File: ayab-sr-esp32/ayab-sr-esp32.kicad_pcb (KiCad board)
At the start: 2 copper layers, 64.5 x 83.1 mm, 65 parts, among them J1 USB_C_Receptacle_USB2.0_16P, J14 Conn_01x08, J2 USB_C_Receptacle_USB2.0_16P, J3 DIN-7, J4 Conn_01x02, Q1 BSS138, U1 CH224A, U10 AP2112K-3.3, U2 USBLC6-2SC6, U3 ESP32-S3-WROOM-1, U4 74AHCT1G125, U5 HS91L02W2C01, U6 TPS54202, U7 INA381A1, U8 74LVC125, U9 TPS54202

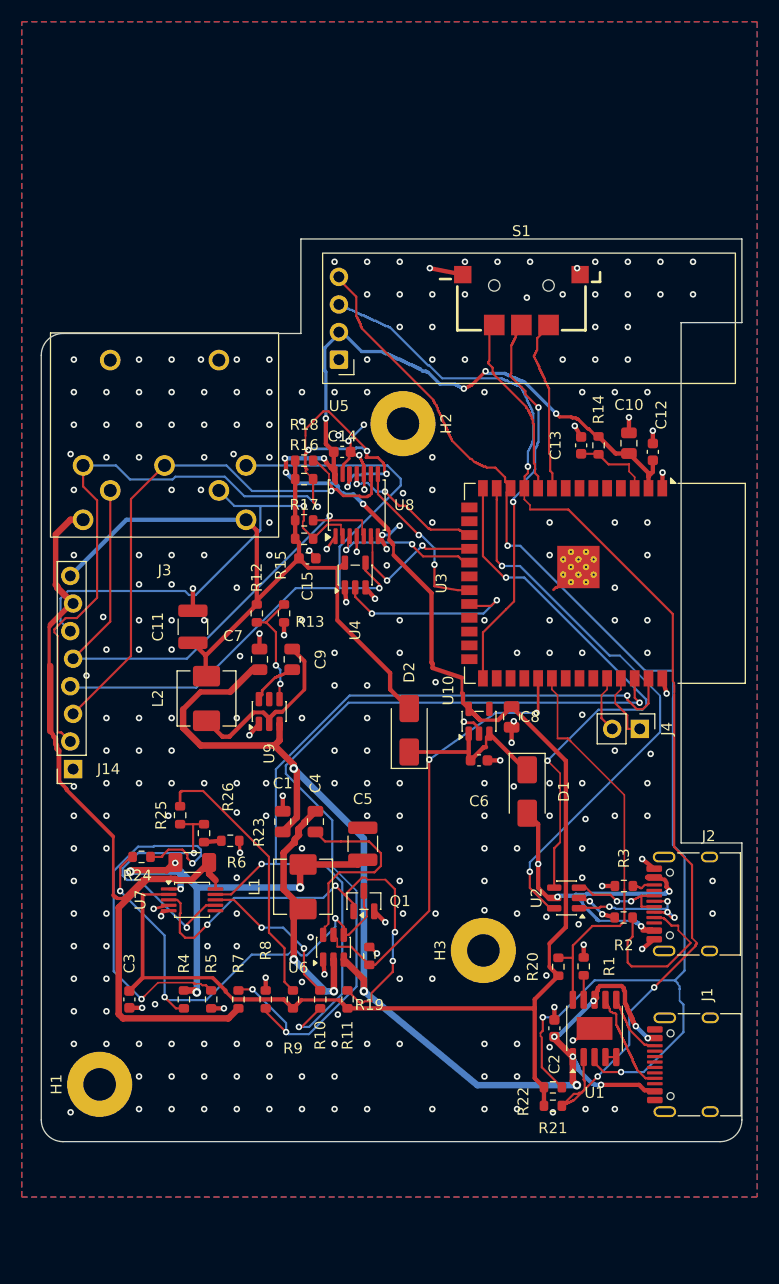
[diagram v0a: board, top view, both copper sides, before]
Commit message: ayab-sr-esp32: board 6 mm longer at the bottom, OLED clear of the antenna keep-out
J3, U5 and S1 and the top edge stay in place; everything else (ESP32 with
its antenna cut-out and keep-out, USB-C, mounting holes...) moves down 6 mm.
Tracks crossing the boundary get vertical extensions; the six DIN-side
tracks cut by it were rerouted. DRC now clean (the U5-in-keep-out item is
gone), connectivity identical. Production files, renders and viewer GLB
regenerated; the enclosure is not updated yet.

Co-Authored-By: Claude Opus 5.5 <noreply@anthropic.com>
Claude-Session: https://claude.ai/code/session_013hjzppJpAsDjhGU3Z3soKr
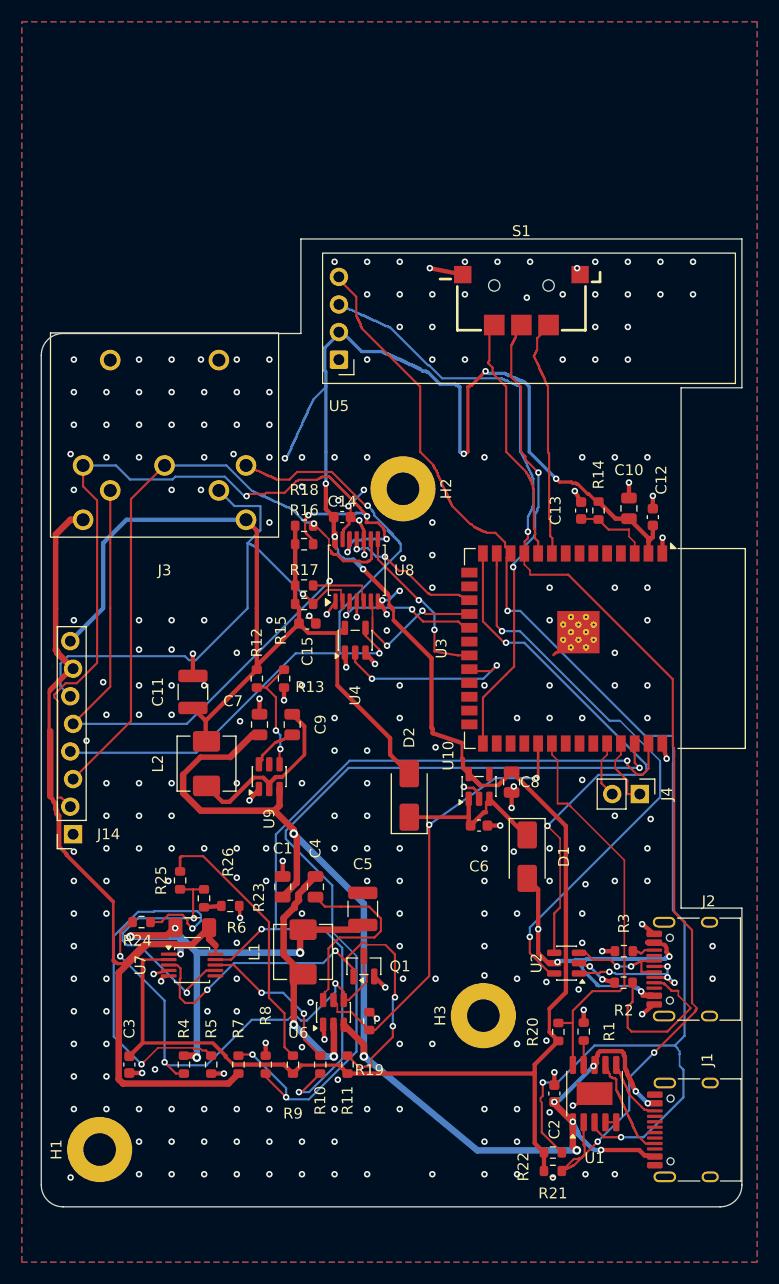
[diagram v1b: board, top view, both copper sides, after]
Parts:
- moved C11 6.00 mm to (114.0, 66.7)
- moved C7 6.00 mm to (120.1, 69.7)
- moved C9 6.00 mm to (123.1, 69.7)
- moved C1 6.00 mm to (122.2, 84.6)
- moved C10 6.00 mm to (154.1, 49.8)
- moved C12 6.00 mm to (156.3, 50.6)
- moved C13 6.00 mm to (149.7, 50.0)
- moved C14 6.00 mm to (127.7, 50.6)
- moved C15 6.00 mm to (124.5, 60.4)
- moved C2 6.00 mm to (147.2, 103.7)
- moved C3 6.00 mm to (108.1, 101.0)
- moved C4 6.00 mm to (125.2, 84.6)
- moved C5 6.00 mm to (129.6, 86.7)
- moved C6 6.00 mm to (140.3, 79.0)
- moved C8 6.00 mm to (143.3, 75.0)
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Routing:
- net +3.3V: track 191.4 -> 214.4 mm, vias 8 -> 7
- net +5V: track 71.9 -> 83.9 mm
- net /ND1: track 87.1 -> 96.4 mm
- net /HOK: track 43.0 -> 50.1 mm
- net /Vsol: track 78.6 -> 84.6 mm
- net /SDA: track 118.2 -> 124.2 mm
- net /CCP: track 52.4 -> 58.4 mm
- net /BTN_D: track 17.1 -> 23.1 mm
- net /BTN_C: track 36.2 -> 42.2 mm
- net /BTN_B: track 16.2 -> 22.2 mm
- net /SCL: track 106.8 -> 112.8 mm
- net /KSL: track 52.7 -> 58.2 mm
- net /DOB: track 62.3 -> 67.4 mm, vias 1 -> 2
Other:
- board size 64.5 x 83.1 mm -> 64.5 x 89.1 mm

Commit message: ayab-sr-esp32: OLED on a low-profile socket, enclosure post under its far end
- J15: 1x4 2.54 mm female socket, 5.0 mm high (HC-PM254-5.0H-1x4PZ-02A,
  LCSC C42163122), on U5's former pads. U5 keeps its symbol (BOM, LCSC
  C5248081) with a pad-less footprint (outline, courtyard, 3D model raised
  5 mm) and is left out of the placement file: it is plugged in by hand.
- New library footprints and a generated STEP model for the socket.
- 3.6 mm hole in the PCB under the OLED's far end (161.0, 32.3) for a
  post of the tray; one GND stitching via removed for edge clearance.
- Enclosure: updated for the 6 mm longer board (holes, USB-C), 3 mm post
  from the tray floor up to 0.1 mm under the module, lid ceiling raised
  by 5 mm (12.8 mm) to clear the OLED glass (11.74 mm). Fit check: no
  collision. Sections redone in the current board frame, plus one through
  the post.
- DRC 0, ERC 0, pad-net check OK; connectivity changes only by J15.
  Production files, renders and viewer regenerated.

Co-Authored-By: Claude Opus 5.5 <noreply@anthropic.com>
Claude-Session: https://claude.ai/code/session_013hjzppJpAsDjhGU3Z3soKr
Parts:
- added J15: HC-PM254-5.0H-1x4PZ-02A, Library:PinSocket_1x04_P2.54mm_Vertical_H5.0, F.Cu at (127.4, 36.1)
- U5: footprint Display:ER_OLEDM0.91_1x-I2C -> Library:OLED_0.91_128x32_I2C_Module_Socket_H5.0
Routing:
- net GND: vias 274 -> 273
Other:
- outline, holes or cut-outs redrawn

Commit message: ayab-sr-esp32: CH224A off the I2C bus, PCB cut under the OLED end, rectangular support block
- U1 CFG2/CFG3 no longer on SCL/SDA (no-connect flags): single-resistor
  mode, R1 alone requests 15 V. The bus serves the OLED only, so the display
  works with only J2 plugged in (an unpowered CH224A would hold the bus at
  ~2 V). Old U1 SDA/SCL tracks removed. Sheet notes and README updated
  (pin map, firmware notes, J2-only operation and PD-adapter-in-J2 detection).
- PCB cut along the antenna cut-out line (x = 158.9) up to the top edge;
  the round post hole is gone. One off-board stitching via removed.
- Enclosure: the OLED's overhanging far end rests on a rectangular block of
  the tray (x 159.3-165.0, y 27.0-37.6, joined to the side wall, 0.1 mm
  under the module). Fit check: no collision. Renders and sections redone.
- DRC 0, ERC 0. Connectivity change: SCL/SDA lose U1.2/U1.3 only.

Co-Authored-By: Claude Opus 5.5 <noreply@anthropic.com>
Claude-Session: https://claude.ai/code/session_013hjzppJpAsDjhGU3Z3soKr
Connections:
- U1 pad 2: /SCL -> unconnected-(U1-CFG2-Pad2)
- U1 pad 3: /SDA -> unconnected-(U1-CFG3-Pad3)
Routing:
- net /SDA: track 124.2 -> 108.5 mm, vias 3 -> 2
- net /SCL: track 112.8 -> 109.8 mm
- net GND: vias 273 -> 272
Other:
- outline, holes or cut-outs redrawn
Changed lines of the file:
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@@
 			(layers "F.Cu" "F.Mask" "F.Paste")
 			(roundrect_rratio 0.25)
-			(net "/SCL")
+			(net "unconnected-(U1-CFG2-Pad2)")
 			(pinfunction "CFG2_2")
-			(pintype "passive")
+			(pintype "passive+no_connect")
 		)
 		(pad "3" smd roundrect
@@
 			(layers "F.Cu" "F.Mask" "F.Paste")
 			(roundrect_rratio 0.25)
-			(net "/SDA")
+			(net "unconnected-(U1-CFG3-Pad3)")
 			(pinfunction "CFG3_3")
-			(pintype "passive")
+			(pintype "passive+no_connect")
 		)
 		(pad "4" smd roundrect
@@
 	(gr_line
 		(start 123.900001 24.999999)
-		(end 164.500001 24.999999)
-		(stroke
-			(width 0.05)
-			(type default)
-		)
-		(layer "Edge.Cuts")
-	)
-	(gr_line
-		(start 158.900001 38.699999)
-		(end 164.500001 38.699999)
+		(end 158.900001 24.999999)
 		(stroke
 			(width 0.05)
@@
 	(gr_line
 		(start 158.900001 86.599999)
-		(end 158.900001 38.699999)
+		(end 158.900001 24.999999)
 		(stroke
 			(width 0.05)
@@
 		(layer "Edge.Cuts")
 	)
-	(gr_circle
-		(center 161 32.3)
-		(end 162.8 32.3)
-		(stroke
-			(width 0.05)
-			(type default)
-		)
-		(fill no)
-		(layer "Edge.Cuts")
-	)
 	(gr_line
 		(start 162.500001 114.099999)
@@
 	)
 	(gr_line
-		(start 164.500001 38.699999)
-		(end 164.500001 24.999999)
-		(stroke
-			(width 0.05)
-			(type default)
-		)
-		(layer "Edge.Cuts")
-	)
-	(gr_line
 		(start 164.500001 86.599999)
 		(end 158.900001 86.599999)
@@
 	)
 	(via
-		(at 160.000001 27.099999)
-		(size 0.6)
-		(drill 0.3)
-		(layers "F.Cu" "B.Cu")
-		(net "GND")
-	)
-	(via
 		(at 118.300001 87.499999)
 		(size 0.6)
@@
 	)
 	(segment
-		(start 149.925001 106.299999)
-		(end 149.925001 108.399999)
-		(width 0.2)
-		(layer "F.Cu")
-		(net "/SCL")
-	)
-	(segment
 		(start 148.825001 110.399999)
 		(end 148.725001 110.399999)
@@
 	)
 	(segment
-		(start 149.925001 108.399999)
-		(end 150.025001 108.499999)
-		(width 0.2)
-		(layer "F.Cu")
-		(net "/SCL")
-	)
-	(segment
 		(start 147.925001 110.799999)
 		(end 149.025001 109.699999)
@@
 	)
 	(segment
-		(start 150.025001 108.499999)
-		(end 150.025001 109.299999)
-		(width 0.2)
-		(layer "F.Cu")
-		(net "/SCL")
-	)
-	(segment
 		(start 158.265001 72.973299)
 		(end 158.276901 72.961399)
@@
 	)
 	(segment
-		(start 150.935001 106.314999)
-		(end 150.935001 106.853899)
-		(width 0.2)
-		(layer "F.Cu")
-		(net "/SDA")
-	)
-	(segment
 		(start 137.700001 49.249999)
 		(end 137.600001 49.149999)
@@
 	)
 	(segment
-		(start 151.775201 107.694099)
-		(end 153.377101 107.694099)
-		(width 0.2)
-		(layer "F.Cu")
-		(net "/SDA")
-	)
-	(segment
 		(start 136.800001 47.249999)
 		(end 136.700001 47.149999)
@@
 	)
 	(segment
-		(start 150.935001 106.853899)
-		(end 151.775201 107.694099)
-		(width 0.2)
-		(layer "F.Cu")
-		(net "/SDA")
-	)
-	(segment
 		(start 129.200001 32.518199)
 		(end 129.200001 32.418199)
@@
 		(net "/SDA")
 	)
-	(via
-		(at 153.377101 107.694099)
-		(size 0.6)
-		(drill 0.3)
-		(layers "F.Cu" "B.Cu")
-		(net "/SDA")
-	)
-	(segment
-		(start 158.848801 101.211099)
-		(end 158.758001 101.120299)
-		(width 0.15)
-		(layer "B.Cu")
-		(net "/SDA")
-	)
-	(segment
-		(start 159.116201 101.478499)
-		(end 158.848801 101.211099)
-		(width 0.2)
-		(layer "B.Cu")
-		(net "/SDA")
-	)
 	(segment
 		(start 147.528401 102.653199)
@@
 	)
 	(segment
-		(start 158.765901 100.051599)
-		(end 158.765901 99.784299)
-		(width 0.2)
-		(layer "B.Cu")
-		(net "/SDA")
-	)
-	(segment
 		(start 150.932901 99.248699)
 		(end 147.528401 102.653199)
@@
 	)
 	(segment
-		(start 158.758001 100.059499)
-		(end 158.765901 100.051599)
-		(width 0.2)
-		(layer "B.Cu")
-		(net "/SDA")
-	)
-	(segment
 		(start 155.593801 70.743599)
 		(end 158.147801 70.743599)
@@
 	)
 	(segment
-		(start 158.758001 101.120299)
-		(end 158.758001 100.059499)
-		(width 0.15)
-		(layer "B.Cu")
-		(net "/SDA")
-	)
-	(segment
 		(start 158.147801 70.743599)
 		(end 158.147801 73.243999)
@@
 	)
 	(segment
-		(start 159.116201 104.020799)
-		(end 159.116201 101.478499)
-		(width 0.2)
-		(layer "B.Cu")
-		(net "/SDA")
-	)
-	(segment
 		(start 158.147801 86.793499)
 		(end 158.147801 73.243999)
@@
 	)
 	(segment
-		(start 153.377101 107.694099)
-		(end 155.442901 107.694099)
-		(width 0.2)
-		(layer "B.Cu")
-		(net "/SDA")
-	)
-	(segment
-		(start 155.442901 107.694099)
-		(end 159.116201 104.020799)
-		(width 0.2)
-		(layer "B.Cu")
-		(net "/SDA")
-	)
-	(segment
-		(start 158.765901 99.784299)
-		(end 158.582301 99.600699)
-		(width 0.15)
-		(layer "B.Cu")
-		(net "/SDA")
-	)
-	(segment
 		(start 158.331001 99.248699)
 		(end 150.932901 99.248699)
@@
 	)
 	(segment
-		(start 158.582301 99.499999)
-		(end 158.331001 99.248699)
-		(width 0.2)
-		(layer "B.Cu")
-		(net "/SDA")
-	)
-	(segment
 		(start 158.331001 99.248699)
 		(end 159.220901 98.358799)
@@
 		(layer "B.Cu")
 		(net "/SDA")
-	)
-	(segment
-		(start 158.582301 99.600699)
-		(end 158.582301 99.499999)
-		(width 0.15)
-		(layer "B.Cu")
-		(net "/SDA")
